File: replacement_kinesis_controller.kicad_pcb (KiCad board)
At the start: 2 copper layers, 99.1 x 99.1 mm, 141 parts, among them CN1 USB_general, CN2 Micro-USB, CN3 Mini-USB, CN4 USB_general, K1 CONN_3, K2 CONN_3, K3 CONN_3, K4 CONN_3, K5 CONN_3, P1 CONN_3X2, P10 CONN_8, P11 CONN_5, P12 CONN_5, P13 CONN_6, P14 CONN_8, P15 CONN_5X2, P16 CONN_16, P17 CONN_16, P18 POWER, P19 PCM, P2 CONN_13, P20 UART, P21 SPI, P22 IO, P23 SMIRF, P24 CONN_2, P25 USB, P3 CONN_13, P4 CONN_10, P5 CONN_10, P6 CONN_13, P7 CONN_13, P8 CONN_5X2, P9 CONN_6, Q1 MOS_P, Q2 MOS_N, Q3 MOS_P, SW1 SW_PUSH, SW2 SW_PUSH, SW3 SPST, SW4 SPST, U1 MCP23018-E, U2 WS2811_RGB_LED, U3 WS2811_RGB_LED, U4 WS2811_RGB_LED, U5 WS2811_RGB_LED, U6 ATmega32U4, U7 WT12-A, U8 MCP73832, U9 MIC5504, X1 16MHz

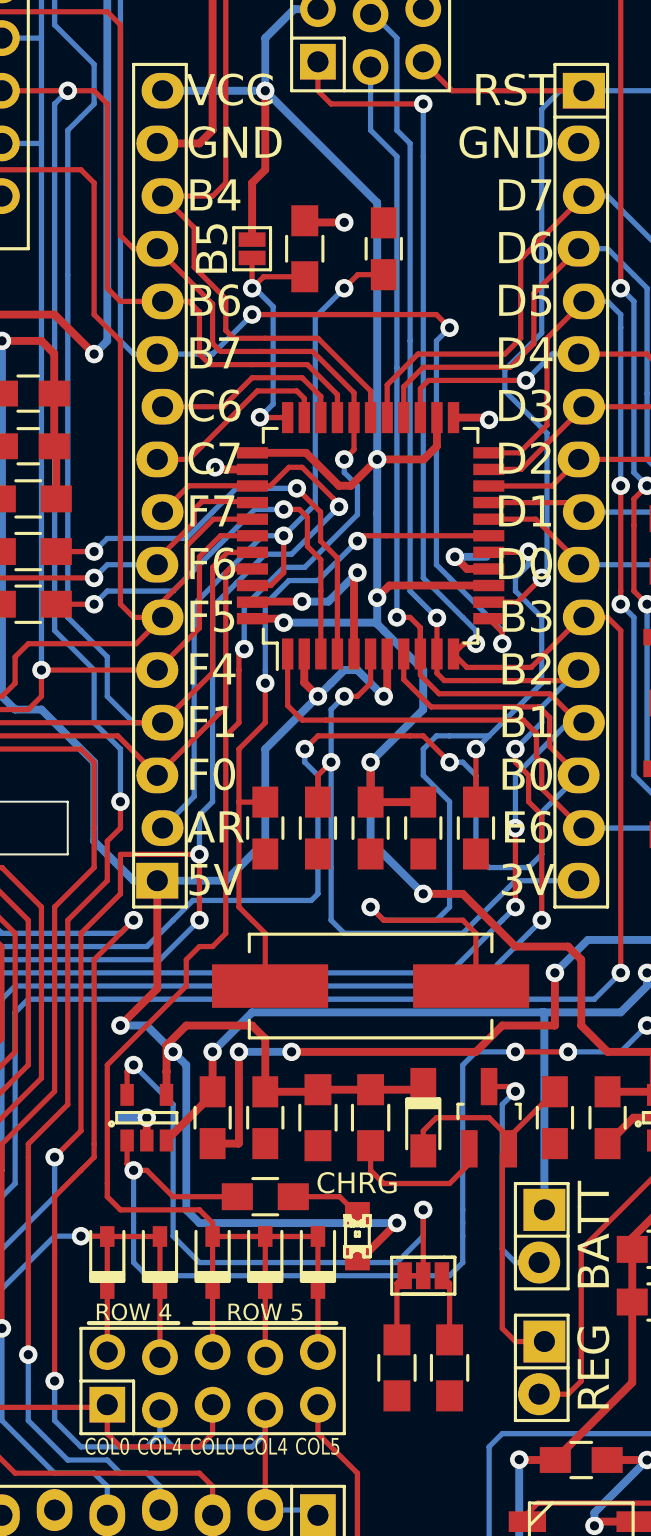
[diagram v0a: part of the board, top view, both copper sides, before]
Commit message: Remove most solder jumpers
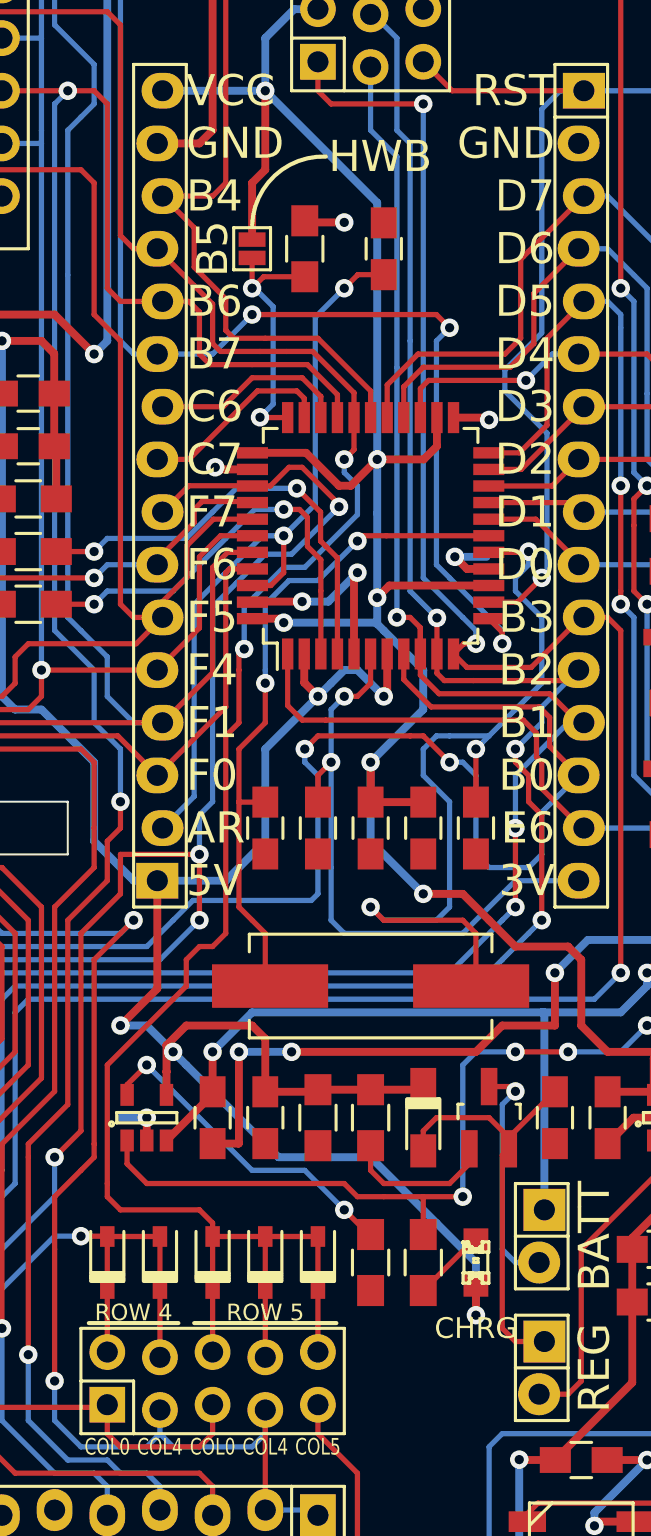
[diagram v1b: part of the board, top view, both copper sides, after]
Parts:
- removed JP3: JUMPER3, replacement_kinesis_controller:JUMPER_3
- removed R19: 10k, Resistors_SMD:R_0805_HandSoldering
- moved R12 8.26 mm to (102.9, 112.4), turned to 270 degrees
- moved D16 5.85 mm to (105.4, 112.4)
- moved R18 5.24 mm to (100.3, 112.4)
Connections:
- net BAT_GUAGE renamed PD6
- net COL_1 renamed PF1
- net COL_5 renamed PF7
- net COL_8 renamed GPB2
- net GPA2 renamed ROW_R2
- net GPB5 renamed COL_11
- net PB0 renamed ROW_L0
- net PB1 renamed ROW_L1
- net PB3 renamed ROW_L3
- net PB4 renamed ROW_L4
- net PD4 renamed LED_DATA
- net PF4 renamed COL_2
- net PF6 renamed COL_4
- net ROW_L2 renamed PB2
- net ROW_L5 renamed PB5
- net ROW_L7 renamed PB7
- net ROW_R6 renamed GPA6
- net SDA renamed PD1
- R10 pad 2: Net-(JP2-Pad2) -> W_PIO5
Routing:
- net W_PIO5: track 59.6 -> 80.2 mm, vias 2 -> 4
- net Net-(JP2-Pad2): track 23.4 -> 2.73 mm, vias 2 -> 0
- net Net-(R18-Pad1): track 32.3 -> 16.0 mm
- net PD7: track 113.2 -> 101.9 mm
- net Net-(JP3-Pad3): track 3.25 -> 0.00 mm
- net +5V: track 113.4 -> 115.3 mm
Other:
- board text added: "HWB"

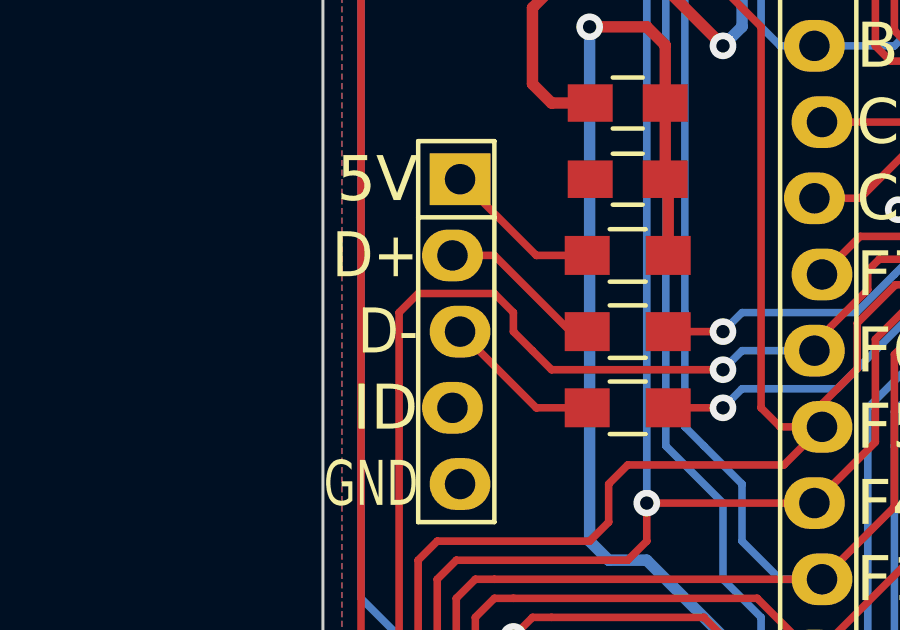
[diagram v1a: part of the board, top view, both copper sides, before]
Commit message: Fix USB pin order on main connector
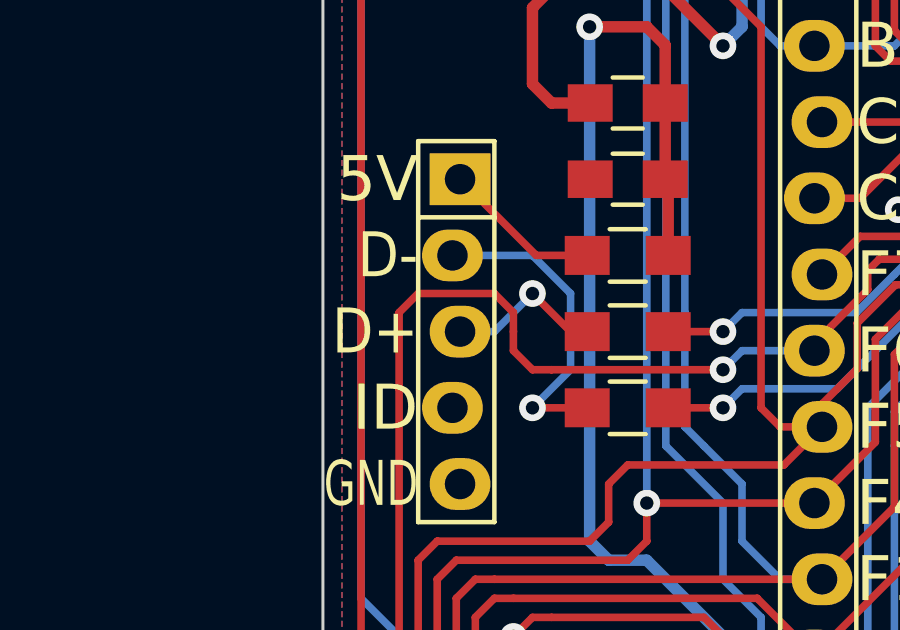
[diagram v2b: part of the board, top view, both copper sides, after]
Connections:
- net COL_10 renamed GPB4
- net COL_3 renamed PF5
- net COL_4 renamed PF6
- net COL_9 renamed GPB3
- net GPA1 renamed ROW_R1
- net GPA4 renamed ROW_R4
- net GPB2 renamed COL_8
- net LED_DATA renamed PD4
- net PD1 renamed SDA
- net PD5 renamed BAT_GUAGE_TOGGLE
- net PD6 renamed BAT_GUAGE
- net PF0 renamed COL_0
- net PF7 renamed COL_5
- net ROW_L1 renamed PB1
- net ROW_L3 renamed PB3
- net ROW_L4 renamed PB4
- net ROW_L6 renamed PB6
- net ROW_R5 renamed GPA5
- net ROW_R7 renamed GPA7
- net SCL renamed PD0
- R8 pad 2: Net-(CN1-Pad2) -> Net-(CN1-Pad3)
- R9 pad 2: Net-(CN1-Pad3) -> Net-(CN1-Pad2)
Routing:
- net Net-(CN1-Pad2): track 5.54 -> 10.6 mm, vias 0 -> 1
- net Net-(CN1-Pad3): vias 0 -> 1
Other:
- board text added: "NC"

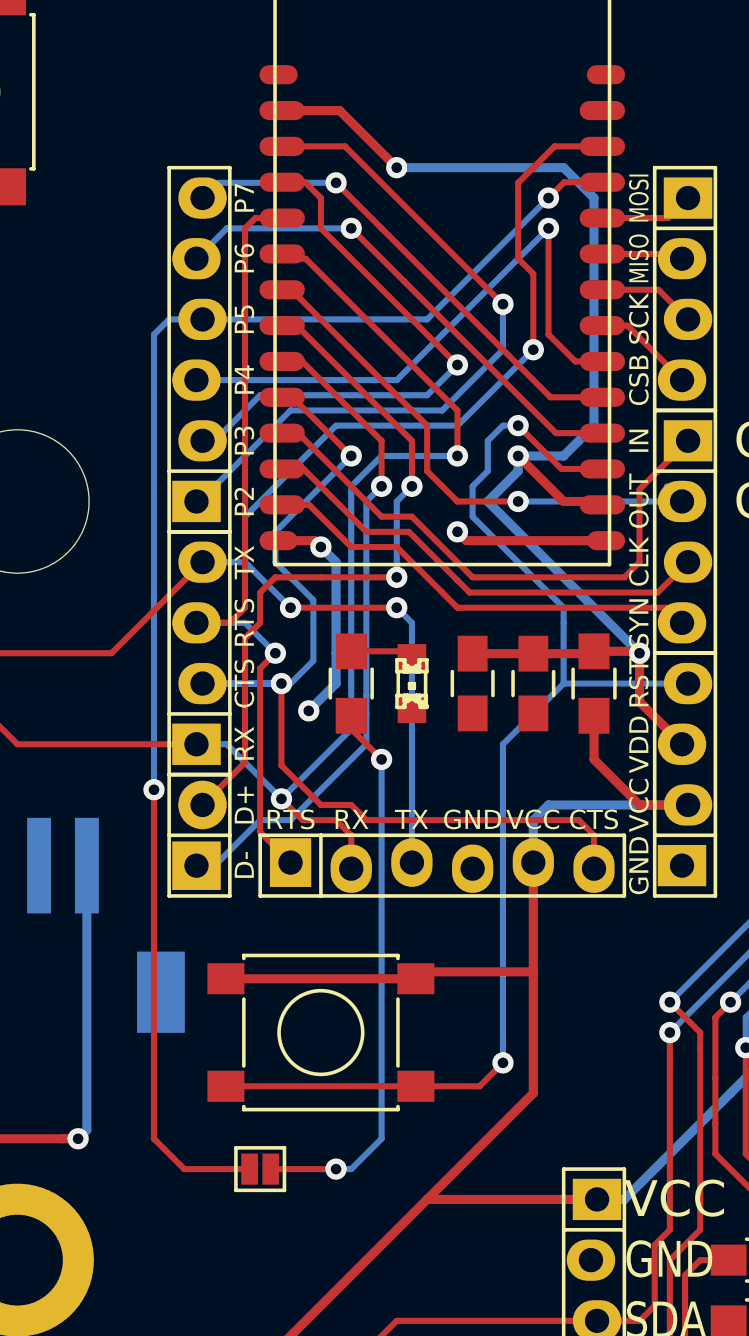
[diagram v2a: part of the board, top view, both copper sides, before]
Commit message: Remove last solder jumper from PCB
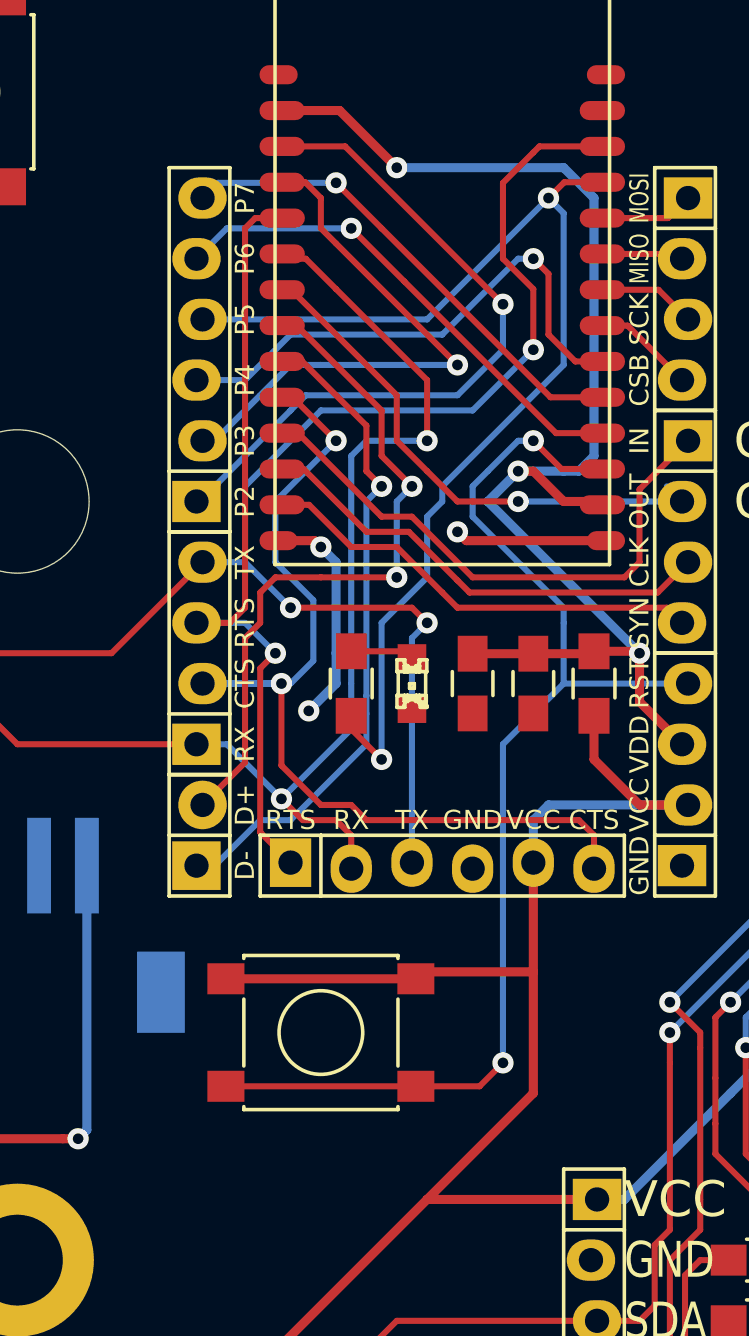
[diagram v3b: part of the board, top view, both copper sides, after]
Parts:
- removed JP2: JUMPER, replacement_kinesis_controller:JUMPER_2
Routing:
- net W_PIO5: track 80.2 -> 48.4 mm, vias 4 -> 2
- net Net-(JP2-Pad2): track 2.73 -> 0.00 mm
- net W_TXD: track 75.3 -> 77.8 mm
- net W_PIO4: track 24.5 -> 22.4 mm
- net PD3: track 70.5 -> 69.1 mm
- net W_RESET: track 52.8 -> 51.6 mm
- net W_NCTS: track 41.9 -> 41.4 mm

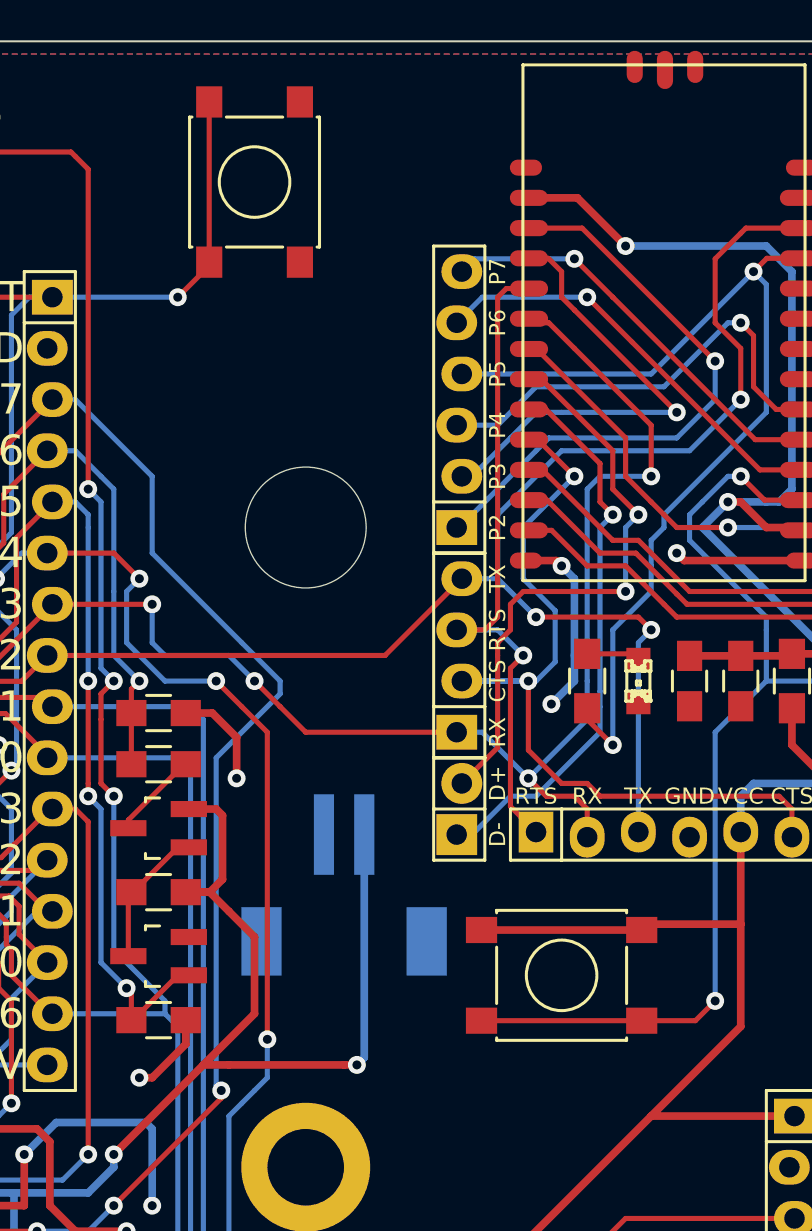
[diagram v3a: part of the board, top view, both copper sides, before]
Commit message: Label reset switches on silk screen
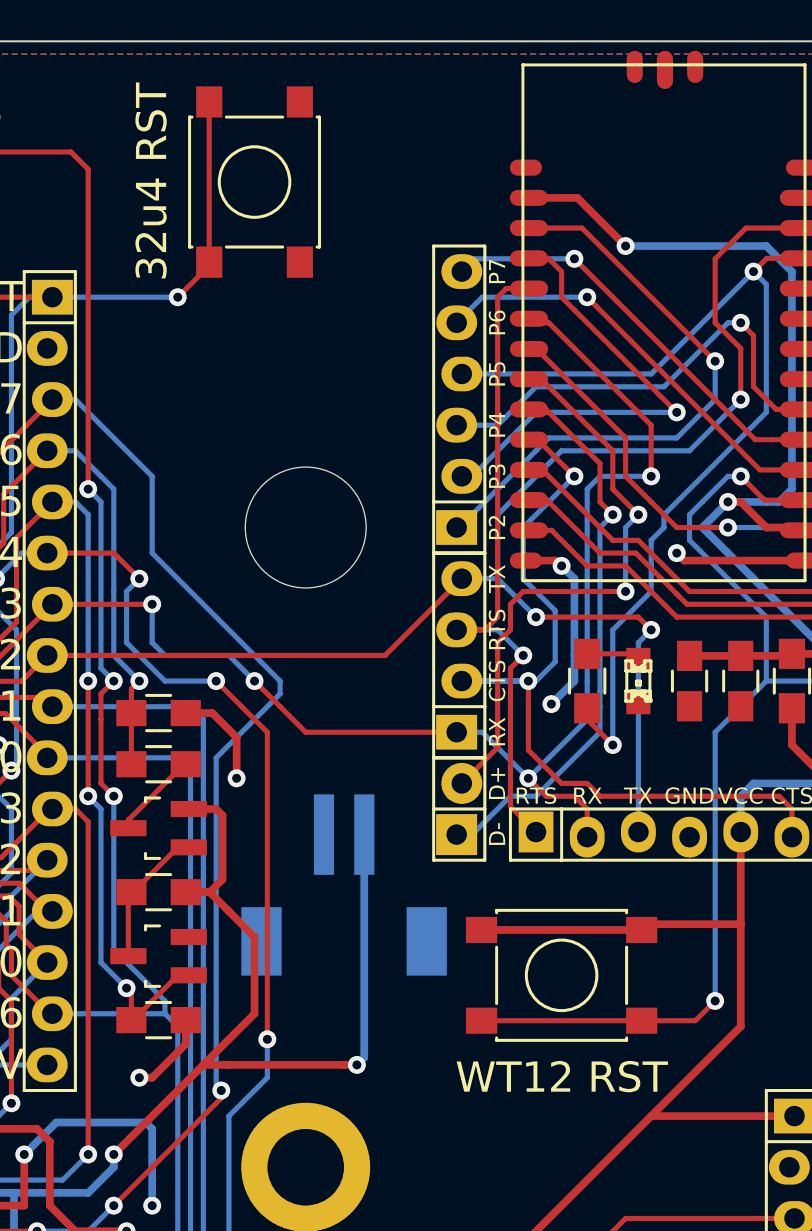
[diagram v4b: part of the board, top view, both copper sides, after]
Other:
- board text added: "32u4 RST"
- board text added: "WT12 RST"
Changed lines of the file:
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@@
     (area 73.609999 43.129999 172.770001 142.290001)
     (thickness 1.6)
-    (drawings 351)
+    (drawings 353)
     (tracks 2181)
     (zones 0)
@@
     )
   )
+  (gr_text "32u4 RST" (at 115.57 50.165 90) (layer F.SilkS)
+    (effects (font (size 1.5 1.5) (thickness 0.3)))
+  )
+  (gr_text "WT12 RST" (at 135.89 94.615) (layer F.SilkS)
+    (effects (font (size 1.5 1.5) (thickness 0.3)))
+  )
   (gr_text NC (at 130.81 135.255) (layer B.SilkS)
